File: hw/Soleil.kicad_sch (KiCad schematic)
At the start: 49 parts, among them J1 Conn_01x04, Q1 MMBT3904, Q2 2N7002, SW1 SW_Push, U1 SPV1040TTR, U2 XS3A1T3157GMX, U3 TPS61220DCK, U4 STM32G030F6Px, U5 ZJY200200-0154DAAMFGN, U6 W25Q16JVUXIQ

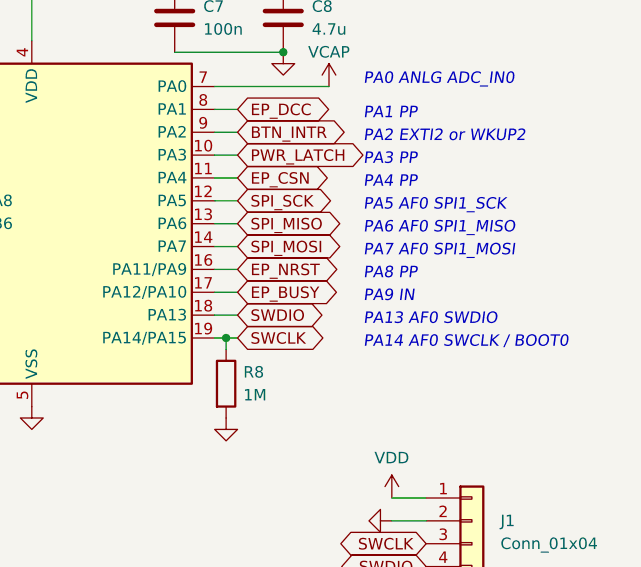
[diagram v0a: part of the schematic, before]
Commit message: (WIP) Adapt firmware pin definitions to Rev. 5 hardware
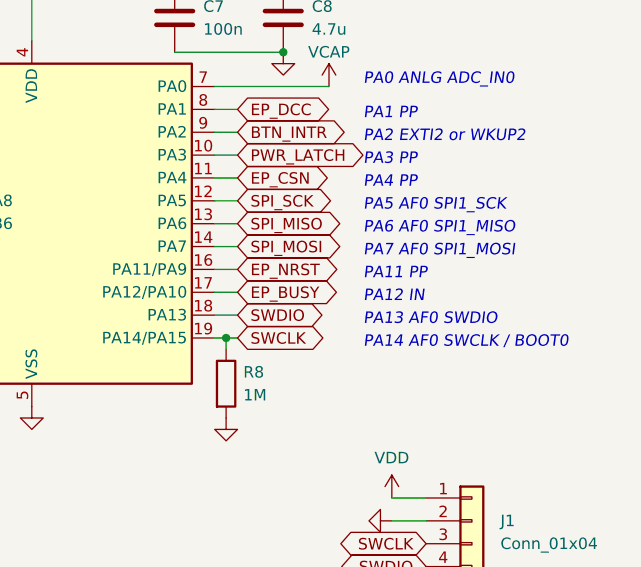
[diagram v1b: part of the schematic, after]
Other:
- note added: "PA11 PP"
- note added: "PA12 IN"
- note removed: "PA8 PP"
- note removed: "PA9 IN"
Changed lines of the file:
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@@
     (stroke (width 0) (type default))
   )
-  (text "PA9 IN" (at 255.905 55.88 0)
+  (text "PA12 IN" (at 255.905 55.88 0)
     (effects (font (size 1.27 1.27) italic) (justify left bottom))
   )
@@
     (effects (font (size 1.27 1.27) italic) (justify right bottom))
   )
-  (text "PA8 PP" (at 255.905 53.34 0)
+  (text "PA11 PP" (at 255.905 53.34 0)
     (effects (font (size 1.27 1.27) italic) (justify left bottom))
   )

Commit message: Revise hardware; fix phantom powering
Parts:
- added Q2: Si2301, Package_TO_SOT_SMD:SOT-23, symbol Device:Q_PMOS_GSD
- added R8, R9: 1M, Resistor_SMD:R_0603_1608Metric, symbol Device:R
- renumbered Q2 to Q3, R8 to R10, R9 to R11, R10 to R12, R11 to R13, R12 to R14
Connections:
- net GND: now also R9.2
- net PWR_LATCH: now also Q2.1 (G), R8.2
- net VCAP: no longer U4.7 (PA0)
- net VRI: now also Q2.2 (S), R8.1
- new net VRI_SENSE: Q2.3 (D), R9.1, U4.7 (PA0)
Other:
- moved on the sheet: C5, C6, L2, R6, R7, U3

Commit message: Revise hardware and submit for fabrication (Rev. 6)
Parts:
- removed Q2: Si2301, Package_TO_SOT_SMD:SOT-23, symbol Device:Q_PMOS_GSD
- removed R8: 1M, Resistor_SMD:R_0603_1608Metric, symbol Device:R
- added Q2: 2N7002, Package_TO_SOT_SMD:SOT-23, symbol Device:Q_NMOS_GSD
- renumbered R11 to R10, R12 to R11, R13 to R12, R14 to R13, R9 to R8, R10 to R9
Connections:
- net GND: now also R5.2, Q2.2 (S); no longer R8.2
- net PWR_LATCH: now also R5.1, Q2.1 (G); no longer R5.2
- net VCAP: now also U2.1 (Y2); no longer R5.1, U2.3 (Y1)
- net VRI: now also R8.1
- net VRI_SENSE: now also R8.2, Q2.3 (D); no longer R8.1
- net at R3.2, SW1.2: now also U2.3 (Y1); no longer U2.1 (Y2)
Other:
- note added: "Already pulled down by R5"
- moved on the sheet: R8

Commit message: Revise schematic
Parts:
- removed C1, C2: 10u, Capacitor_SMD:C_0603_1608Metric, symbol Device:C
- removed L1: 10u, Inductor_SMD:L_Sunlord_SWPA252012S, symbol Device:L
- removed R1: 360k, Resistor_SMD:R_0603_1608Metric, symbol Device:R
- removed R2: 220k, Resistor_SMD:R_0603_1608Metric, symbol Device:R
- removed R9: 1M, Resistor_SMD:R_0603_1608Metric, symbol Device:R
- removed U1: SPV1040TTR, Package_SO:TSSOP-8_4.4x3mm_P0.65mm, symbol Soleil_symbols:SPV1040TTR
- added C4: 220m, Soleil_footprints:DMS3R3, symbol Device:C_Polarized
- added C6, C8: 10u, Capacitor_SMD:C_0603_1608Metric, symbol Device:C
- added C7: 100n, Capacitor_SMD:C_0603_1608Metric, symbol Device:C
- added C9: 2.2u, Capacitor_SMD:C_0603_1608Metric, symbol Device:C
- added L2: 10u, Inductor_SMD:L_Sunlord_SWPA252012S, symbol Device:L
- added R6: 560k, Resistor_SMD:R_0402_1005Metric, symbol Device:R
- added R7: 100k, Resistor_SMD:R_0402_1005Metric, symbol Device:R
- added R8: 1, Resistor_SMD:R_0402_1005Metric, symbol Device:R
- added U3: TPS61020DRCR, Soleil_footprints:TPS61020DRCR, symbol Soleil_symbols:TPS61020DRCR
- renumbered C5 to C1, C7 to C10, C8 to C11, C9 to C12, C10 to C13, C11 to C14, C12 to C15, C13 to C16, C14 to C17, C15 to C18, C16 to C19, C6 to C2, C17 to C20, C18 to C21, C19 to C22, C4 to C5, L2 to L1, R6 to R1, R7 to R2, R8 to R9, U3 to U1
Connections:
- net GND: now also C4.2, C6.2, C7.2, C9.2, R7.2, R8.2, U3.10 (PGND), U3.11 (EP/PGND_1), U3.5 (GND), U3.7 (LBI), U3.8 (PS), U3.A11 (EP/PGND_2), U3.B11 (EP/PGND_3), U3.C11 (EP/PGND_4), U3.D11 (EP/PGND_5)
- net VCAP: now also C2.1, R1.1, U1.4 (VOUT), C4.1
- net VDD: now also C8.1, C9.1, R6.1, U3.2 (VOUT); no longer C2.1, R1.1, U1.4 (VOUT)
- net VRI: now also C6.1, C7.1, L2.1, U3.1 (EN), U3.6 (VBAT); no longer C1.1, L1.1, U1.1 (VIN), U1.6 (EN)
- net at SC1.1 (+): now also C1.1, L1.1, U1.1 (VIN), U1.6 (EN)
- new net: L2.2, U3.9 (SW)
- new net: R6.2, R7.1, U3.3 (FB)
- new net: C8.2, R8.1
- no-connect marks 6 -> 7
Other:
- note removed: "R1 = R2 × (V_OUT / V_FB - 1) V_FB = 1.25 V typ."
- moved on the sheet: C1, C2, C3, C5, L1, R1, R2, U1

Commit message: Update layout, 🚧 routing to-do
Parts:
- C10, C11, C12, C13, C14, C15, C16, C17, C18, C19, C20, C21, C22, C5, C7, C9: footprint Capacitor_SMD:C_0603_1608Metric -> Capacitor_SMD:C_0402_1005Metric
- R1, R10, R11, R12, R13, R2, R3, R4, R5, R9: footprint Resistor_SMD:R_0603_1608Metric -> Resistor_SMD:R_0402_1005Metric
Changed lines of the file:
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@@
       (effects (font (size 1.27 1.27)))
     )
-    (property "Footprint" "Capacitor_SMD:C_0603_1608Metric" (at 114.935 131.1148 0)
+    (property "Footprint" "Capacitor_SMD:C_0402_1005Metric" (at 114.935 131.1148 0)
       (effects (font (size 1.27 1.27)) hide)
     )
@@
       (effects (font (size 1.27 1.27)))
     )
-    (property "Footprint" "Resistor_SMD:R_0603_1608Metric" (at 34.29 101.092 90)
+    (property "Footprint" "Resistor_SMD:R_0402_1005Metric" (at 34.29 101.092 90)
       (effects (font (size 1.27 1.27)) hide)
     )
@@
       (effects (font (size 1.27 1.27)) (justify left))
     )
-    (property "Footprint" "Resistor_SMD:R_0603_1608Metric" (at 83.312 38.735 90)
+    (property "Footprint" "Resistor_SMD:R_0402_1005Metric" (at 83.312 38.735 90)
       (effects (font (size 1.27 1.27)) hide)
     )
@@
       (effects (font (size 1.27 1.27)))
     )
-    (property "Footprint" "Capacitor_SMD:C_0603_1608Metric" (at 111.125 171.7548 0)
+    (property "Footprint" "Capacitor_SMD:C_0402_1005Metric" (at 111.125 171.7548 0)
       (effects (font (size 1.27 1.27)) hide)
     )
@@
       (effects (font (size 1.27 1.27)) (justify right))
     )
-    (property "Footprint" "Capacitor_SMD:C_0603_1608Metric" (at 233.9848 20.32 0)
+    (property "Footprint" "Capacitor_SMD:C_0402_1005Metric" (at 233.9848 20.32 0)
       (effects (font (size 1.27 1.27)) hide)
     )
@@
       (effects (font (size 1.27 1.27)) (justify left))
     )
-    (property "Footprint" "Capacitor_SMD:C_0603_1608Metric" (at 116.5098 82.55 0)
+    (property "Footprint" "Capacitor_SMD:C_0402_1005Metric" (at 116.5098 82.55 0)
       (effects (font (size 1.27 1.27)) hide)
     )
@@
       (effects (font (size 1.27 1.27)) (justify left))
     )
-    (property "Footprint" "Capacitor_SMD:C_0603_1608Metric" (at 57.4548 139.7 0)
+    (property "Footprint" "Capacitor_SMD:C_0402_1005Metric" (at 57.4548 139.7 0)
       (effects (font (size 1.27 1.27)) hide)
     )
@@
       (effects (font (size 1.27 1.27)))
     )
-    (property "Footprint" "Capacitor_SMD:C_0603_1608Metric" (at 116.84 169.2148 0)
+    (property "Footprint" "Capacitor_SMD:C_0402_1005Metric" (at 116.84 169.2148 0)
       (effects (font (size 1.27 1.27)) hide)
     )
@@
       (effects (font (size 1.27 1.27)) (justify left))
     )
-    (property "Footprint" "Capacitor_SMD:C_0603_1608Metric" (at 185.7502 82.55 0)
+    (property "Footprint" "Capacitor_SMD:C_0402_1005Metric" (at 185.7502 82.55 0)
       (effects (font (size 1.27 1.27)) hide)
     )
@@
       (effects (font (size 1.27 1.27)) (justify right))
     )
-    (property "Footprint" "Capacitor_SMD:C_0603_1608Metric" (at 272.0848 116.84 0)
+    (property "Footprint" "Capacitor_SMD:C_0402_1005Metric" (at 272.0848 116.84 0)
       (effects (font (size 1.27 1.27)) hide)
     )
@@
       (effects (font (size 1.27 1.27)) (justify left))
     )
-    (property "Footprint" "Capacitor_SMD:C_0603_1608Metric" (at 32.6898 148.59 0)
+    (property "Footprint" "Capacitor_SMD:C_0402_1005Metric" (at 32.6898 148.59 0)
       (effects (font (size 1.27 1.27)) hide)
     )
@@
       (effects (font (size 1.27 1.27)))
     )
-    (property "Footprint" "Capacitor_SMD:C_0603_1608Metric" (at 106.68 164.1348 0)
+    (property "Footprint" "Capacitor_SMD:C_0402_1005Metric" (at 106.68 164.1348 0)
       (effects (font (size 1.27 1.27)) hide)
     )
@@
       (effects (font (size 1.27 1.27)) (justify right))
     )
-    (property "Footprint" "Capacitor_SMD:C_0603_1608Metric" (at 84.1502 73.025 0)
+    (property "Footprint" "Capacitor_SMD:C_0402_1005Metric" (at 84.1502 73.025 0)
       (effects (font (size 1.27 1.27)) hide)
     )
@@
       (effects (font (size 1.27 1.27)) (justify left))
     )
-    (property "Footprint" "Resistor_SMD:R_0603_1608Metric" (at 56.642 160.02 90)
+    (property "Footprint" "Resistor_SMD:R_0402_1005Metric" (at 56.642 160.02 90)
       (effects (font (size 1.27 1.27)) hide)
     )
@@
       (effects (font (size 1.27 1.27)) (justify left))
     )
-    (property "Footprint" "Resistor_SMD:R_0603_1608Metric" (at 223.012 83.82 90)
+    (property "Footprint" "Resistor_SMD:R_0402_1005Metric" (at 223.012 83.82 90)
       (effects (font (size 1.27 1.27)) hide)
     )
@@
       (effects (font (size 1.27 1.27)) (justify left))
     )
-    (property "Footprint" "Resistor_SMD:R_0603_1608Metric" (at 83.312 29.845 90)
+    (property "Footprint" "Resistor_SMD:R_0402_1005Metric" (at 83.312 29.845 90)
       (effects (font (size 1.27 1.27)) hide)
     )
@@
       (effects (font (size 1.27 1.27)))
     )
-    (property "Footprint" "Resistor_SMD:R_0603_1608Metric" (at 210.82 149.098 90)
+    (property "Footprint" "Resistor_SMD:R_0402_1005Metric" (at 210.82 149.098 90)
       (effects (font (size 1.27 1.27)) hide)
     )
@@
       (effects (font (size 1.27 1.27)))
     )
-    (property "Footprint" "Resistor_SMD:R_0603_1608Metric" (at 69.977 63.5 90)
+    (property "Footprint" "Resistor_SMD:R_0402_1005Metric" (at 69.977 63.5 90)
       (effects (font (size 1.27 1.27)) hide)
     )
@@
       (effects (font (size 1.27 1.27)) (justify right))
     )
-    (property "Footprint" "Capacitor_SMD:C_0603_1608Metric" (at 246.0498 20.32 0)
+    (property "Footprint" "Capacitor_SMD:C_0402_1005Metric" (at 246.0498 20.32 0)
       (effects (font (size 1.27 1.27)) hide)
     )
@@
       (effects (font (size 1.27 1.27)) (justify right))
     )
-    (property "Footprint" "Resistor_SMD:R_0603_1608Metric" (at 43.942 91.44 90)
+    (property "Footprint" "Resistor_SMD:R_0402_1005Metric" (at 43.942 91.44 90)
       (effects (font (size 1.27 1.27)) hide)
     )
@@
       (effects (font (size 1.27 1.27)))
     )
-    (property "Footprint" "Resistor_SMD:R_0603_1608Metric" (at 210.82 159.258 90)
+    (property "Footprint" "Resistor_SMD:R_0402_1005Metric" (at 210.82 159.258 90)
       (effects (font (size 1.27 1.27)) hide)
     )
@@
       (effects (font (size 1.27 1.27)))
     )
-    (property "Footprint" "Capacitor_SMD:C_0603_1608Metric" (at 116.84 179.3748 0)
+    (property "Footprint" "Capacitor_SMD:C_0402_1005Metric" (at 116.84 179.3748 0)
       (effects (font (size 1.27 1.27)) hide)
     )
@@
       (effects (font (size 1.27 1.27)))
     )
-    (property "Footprint" "Capacitor_SMD:C_0603_1608Metric" (at 106.68 156.5148 0)
+    (property "Footprint" "Capacitor_SMD:C_0402_1005Metric" (at 106.68 156.5148 0)
       (effects (font (size 1.27 1.27)) hide)
     )
@@
       (effects (font (size 1.27 1.27)))
     )
-    (property "Footprint" "Capacitor_SMD:C_0603_1608Metric" (at 116.84 174.2948 0)
+    (property "Footprint" "Capacitor_SMD:C_0402_1005Metric" (at 116.84 174.2948 0)
       (effects (font (size 1.27 1.27)) hide)
     )
@@
       (effects (font (size 1.27 1.27)))
     )
-    (property "Footprint" "Resistor_SMD:R_0603_1608Metric" (at 210.82 154.178 90)
+    (property "Footprint" "Resistor_SMD:R_0402_1005Metric" (at 210.82 154.178 90)
       (effects (font (size 1.27 1.27)) hide)
     )
@@
       (effects (font (size 1.27 1.27)))
     )
-    (property "Footprint" "Capacitor_SMD:C_0603_1608Metric" (at 111.125 176.8348 0)
-      (effects (font (size 1.27 1.27)) hide)
-    )
+    (property "Footprint" "Capacitor_SMD:C_0402_1005Metric" (at 111.125 176.8348 0)
+      (effects (font (size 1.27 1.27)) hide)
+    )

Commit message: Finish board routing
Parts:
- C1, C2, C6, C8: footprint Capacitor_SMD:C_0603_1608Metric -> Capacitor_SMD:C_0402_1005Metric
- R3: value 470k -> 1M
- R4: value 470k -> 100k
- R6: value 560k -> 1M
- R7: value 100k -> 200k
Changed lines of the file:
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@@
       (effects (font (size 1.27 1.27)))
     )
-    (property "Value" "470k" (at 34.29 100.33 90)
+    (property "Value" "1M" (at 34.29 100.33 90)
       (effects (font (size 1.27 1.27)))
     )
@@
       (effects (font (size 1.27 1.27)) (justify left))
     )
-    (property "Footprint" "Capacitor_SMD:C_0603_1608Metric" (at 96.8502 36.195 0)
+    (property "Footprint" "Capacitor_SMD:C_0402_1005Metric" (at 96.8502 36.195 0)
       (effects (font (size 1.27 1.27)) hide)
     )
@@
       (effects (font (size 1.27 1.27)) (justify left))
     )
-    (property "Footprint" "Capacitor_SMD:C_0603_1608Metric" (at 174.9552 77.47 0)
+    (property "Footprint" "Capacitor_SMD:C_0402_1005Metric" (at 174.9552 77.47 0)
       (effects (font (size 1.27 1.27)) hide)
     )
@@
       (effects (font (size 1.27 1.27)) (justify left))
     )
-    (property "Footprint" "Capacitor_SMD:C_0603_1608Metric" (at 45.4152 38.735 0)
+    (property "Footprint" "Capacitor_SMD:C_0402_1005Metric" (at 45.4152 38.735 0)
       (effects (font (size 1.27 1.27)) hide)
     )
@@
       (effects (font (size 1.27 1.27)) (justify right))
     )
-    (property "Value" "470k" (at 43.18 92.71 0)
+    (property "Value" "100k" (at 43.18 92.71 0)
       (effects (font (size 1.27 1.27)) (justify right))
     )
@@
   )
   (symbol (lib_id "Device:R") (at 163.195 73.66 0) (unit 1)
-    (in_bom yes) (on_board yes) (dnp no) (fields_autoplaced)
+    (in_bom yes) (on_board yes) (dnp no)
     (property "Reference" "R6" (at 165.735 72.39 0)
       (effects (font (size 1.27 1.27)) (justify left))
     )
-    (property "Value" "560k" (at 165.735 74.93 0)
+    (property "Value" "1M" (at 165.735 74.93 0)
       (effects (font (size 1.27 1.27)) (justify left))
     )
@@
   )
   (symbol (lib_id "Device:R") (at 163.195 82.55 0) (unit 1)
-    (in_bom yes) (on_board yes) (dnp no) (fields_autoplaced)
+    (in_bom yes) (on_board yes) (dnp no)
     (property "Reference" "R7" (at 165.735 81.28 0)
       (effects (font (size 1.27 1.27)) (justify left))
     )
-    (property "Value" "100k" (at 165.735 83.82 0)
+    (property "Value" "200k" (at 165.735 83.82 0)
       (effects (font (size 1.27 1.27)) (justify left))
     )
@@
       (effects (font (size 1.27 1.27)) (justify left))
     )
-    (property "Footprint" "Capacitor_SMD:C_0603_1608Metric" (at 105.7148 82.55 0)
-      (effects (font (size 1.27 1.27)) hide)
-    )
+    (property "Footprint" "Capacitor_SMD:C_0402_1005Metric" (at 105.7148 82.55 0)
+      (effects (font (size 1.27 1.27)) hide)
+    )

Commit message: Finish board update; submit for fab (Rev. 7)
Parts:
- R1: value 560k -> 1M
- R2: value 100k -> 180k
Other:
- note added: "Programmed V_OUT = 3.28 V"
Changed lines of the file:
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@@
     (effects (font (size 1.27 1.27) italic) (justify left bottom))
   )
-  (text "Programmed V_OUT = 3.3 V" (at 81.28 24.765 0)
+  (text "Programmed V_OUT = 3.28 V" (at 81.28 24.765 0)
     (effects (font (size 1.27 1.27) italic) (justify left bottom))
   )
@@
       (effects (font (size 1.27 1.27)) (justify left))
     )
-    (property "Value" "100k" (at 87.63 40.005 0)
+    (property "Value" "180k" (at 87.63 40.005 0)
       (effects (font (size 1.27 1.27)) (justify left))
     )
@@
       (effects (font (size 1.27 1.27)) (justify left))
     )
-    (property "Value" "560k" (at 87.63 31.115 0)
-      (effects (font (size 1.27 1.27)) (justify left))
-    )
+    (property "Value" "1M" (at 87.63 31.115 0)
+      (effects (font (size 1.27 1.27)) (justify left))
+    )

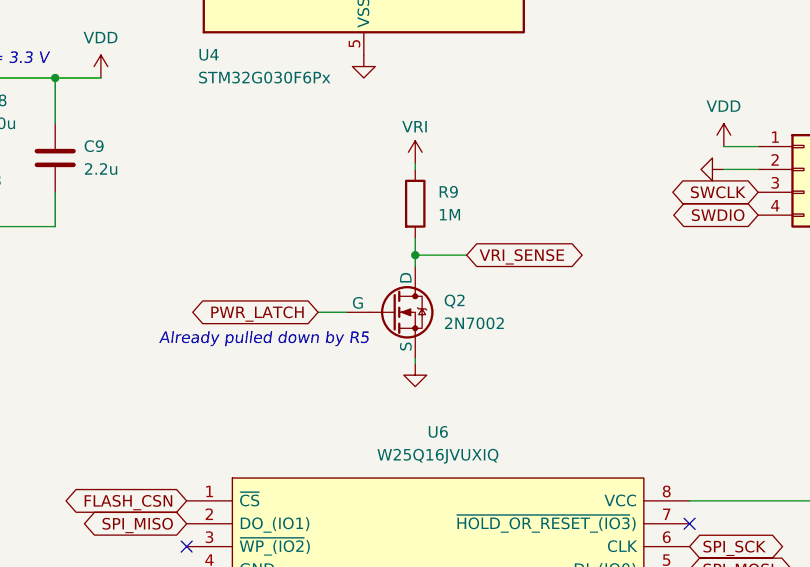
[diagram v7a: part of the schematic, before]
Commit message: Correctly read ADC value
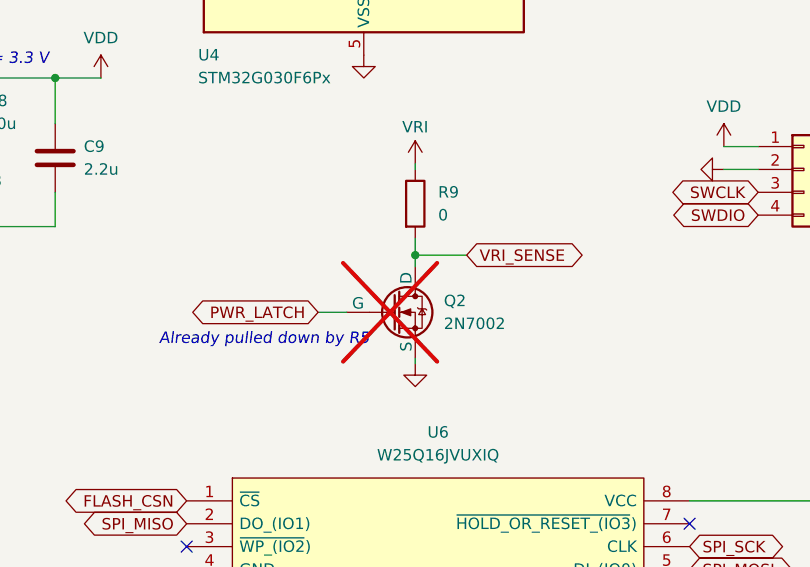
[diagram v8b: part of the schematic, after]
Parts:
- Q2: now not fitted
- R9: value 1M -> 0
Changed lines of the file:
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@@
       (effects (font (size 1.27 1.27)) (justify left))
     )
-    (property "Value" "1M" (at 227.33 85.09 0)
+    (property "Value" "0" (at 227.33 85.09 0)
       (effects (font (size 1.27 1.27)) (justify left))
     )
@@
   )
   (symbol (lib_id "Device:Q_NMOS_GSD") (at 222.25 95.885 0) (unit 1)
-    (in_bom yes) (on_board yes) (dnp no)
+    (in_bom yes) (on_board yes) (dnp yes)
     (property "Reference" "Q2" (at 227.965 94.615 0)
       (effects (font (size 1.27 1.27)) (justify left))
